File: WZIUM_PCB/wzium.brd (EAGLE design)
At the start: 100 x 100 mm, 9 parts, among them J1 RASPBERRYPI-40-PIN-GPIO_PTH

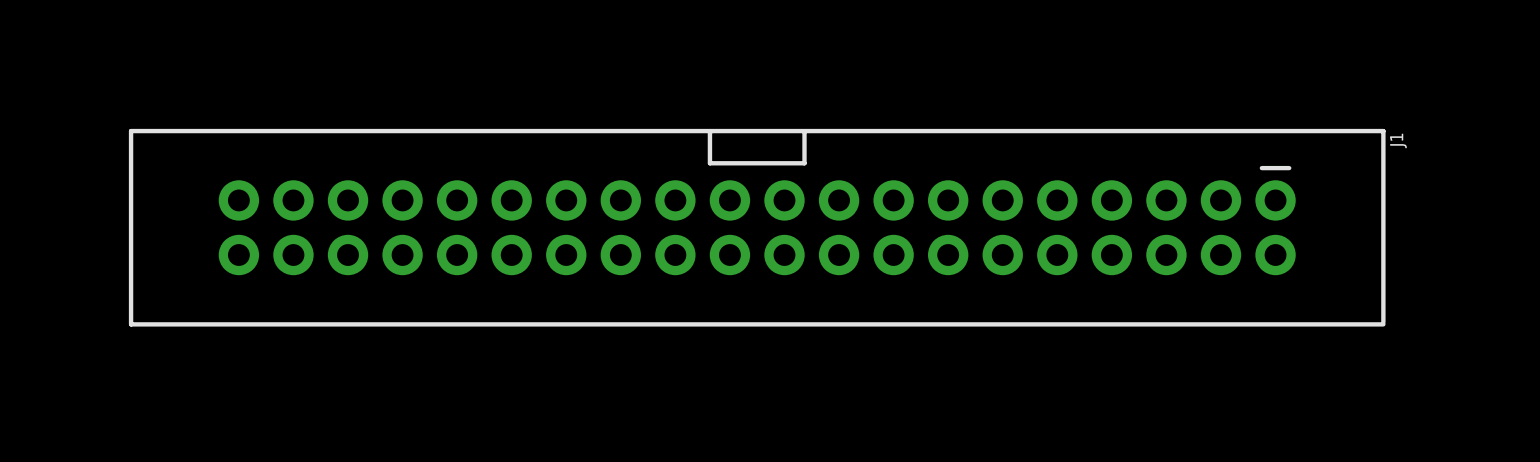
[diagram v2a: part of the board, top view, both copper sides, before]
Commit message: [FIX][ADD][PCB] Naprawiłem kolejnośc pinów od RPi na PCB | dodałem obrys RPi,
piny od RPi na 100% będą właśnie w tej konfiguracji. Obrazek na płytce póki co może być mylący, bo gniazdo FC 40p powinno mieć "ząbek" po drugiej stronie, ale postaram się to naprawić później. Dodałem też obrys RPi, dla łatwiejszego wyobrażania sobie jak to będzie wyglądało.
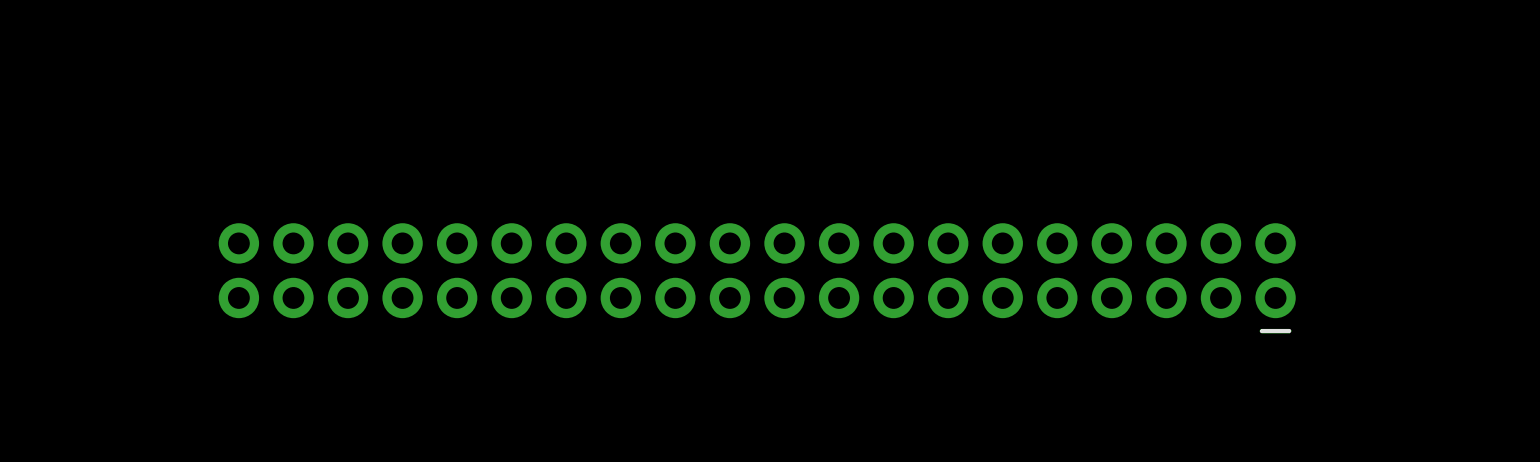
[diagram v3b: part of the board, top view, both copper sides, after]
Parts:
- moved J1 2.00 mm to (44.0, 41.0), flipped to the bottom, turned to 90 degrees
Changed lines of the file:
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@@
 <dimension x1="14.675" y1="77.375" x2="14.725" y2="28.375" x3="-2" y3="52.875" textsize="1.016" layer="1" dtype="vertical" width="0.05"/>
 <dimension x1="14.8" y1="75.775" x2="14.7" y2="29.975" x3="2" y3="52.875" textsize="1.016" layer="1" dtype="vertical" width="0.05"/>
+<wire x1="-8.825" y1="24.875" x2="-8.825" y2="80.875" width="0.1" layer="49"/>
+<wire x1="-8.825" y1="80.875" x2="76.175" y2="80.875" width="0.1" layer="49"/>
+<wire x1="76.175" y1="80.875" x2="76.175" y2="24.875" width="0.1" layer="49"/>
+<wire x1="76.175" y1="24.875" x2="-8.825" y2="24.875" width="0.1" layer="49"/>
 </plain>
 <attributes>
@@
 </autorouter>
 <elements>
-<element name="J1" library="SparkFun-Connectors" library_urn="urn:adsk.eagle:library:513" package="2X20_SHROUDED" package3d_urn="urn:adsk.eagle:package:38279/1" value="RASPBERRYPI-40-PIN-GPIO_PTH" x="44" y="43" smashed="yes" rot="R270">
-<attribute name="NAME" x="73.464" y="47.445" size="0.6096" layer="25" font="vector" ratio="20" rot="R270"/>
-<attribute name="PROD_ID" value="CONN-12263" x="44" y="43" size="1.778" layer="27" rot="R270" display="off"/>
-<attribute name="SF_ID" value="PRT-13054" x="44" y="43" size="1.778" layer="27" rot="R270" display="off"/>
-<attribute name="VALUE" x="13.901" y="47.318" size="0.6096" layer="27" font="vector" ratio="20" rot="R270"/>
+<element name="J1" library="SparkFun-Connectors" library_urn="urn:adsk.eagle:library:513" package="2X20_SHROUDED" package3d_urn="urn:adsk.eagle:package:38279/1" value="RASPBERRYPI-40-PIN-GPIO_PTH" x="44" y="41" smashed="yes" rot="MR90">
+<attribute name="NAME" x="73.464" y="36.555" size="0.6096" layer="26" font="vector" ratio="20" rot="MR90"/>
+<attribute name="PROD_ID" value="CONN-12263" x="44" y="41" size="1.778" layer="28" rot="MR90" display="off"/>
+<attribute name="SF_ID" value="PRT-13054" x="44" y="41" size="1.778" layer="28" rot="MR90" display="off"/>
+<attribute name="VALUE" x="13.901" y="36.682" size="0.6096" layer="28" font="vector" ratio="20" rot="MR90"/>
 </element>
 <element name="X1" library="con-yamaichi" library_urn="urn:adsk.eagle:library:202" package="USB-A003" package3d_urn="urn:adsk.eagle:package:11805/1" value="" x="59" y="101" smashed="yes" rot="R180">
@@
 <contactref element="J1" pad="1"/>
 <contactref element="J1" pad="17"/>
-<wire x1="47.81" y1="44.27" x2="68.13" y2="44.27" width="0" layer="19" extent="1-1"/>
+<wire x1="47.81" y1="39.73" x2="68.13" y2="39.73" width="0" layer="19" extent="1-1"/>
 </signal>
 <signal name="GND">
@@
 <contactref element="X1" pad="1"/>
 <wire x1="44.05" y1="81" x2="62.5" y2="87" width="0" layer="19" extent="1-1"/>
-<wire x1="37.65" y1="44.27" x2="44.05" y2="81" width="0" layer="19" extent="1-1"/>
-<wire x1="32.57" y1="41.73" x2="37.65" y2="44.27" width="0" layer="19" extent="1-1"/>
-<wire x1="27.49" y1="41.73" x2="32.57" y2="41.73" width="0" layer="19" extent="1-1"/>
-<wire x1="45.27" y1="41.73" x2="37.65" y2="44.27" width="0" layer="19" extent="1-1"/>
-<wire x1="52.89" y1="41.73" x2="45.27" y2="41.73" width="0" layer="19" extent="1-1"/>
-<wire x1="57.97" y1="44.27" x2="52.89" y2="41.73" width="0" layer="19" extent="1-1"/>
-<wire x1="63.05" y1="41.73" x2="57.97" y2="44.27" width="0" layer="19" extent="1-1"/>
-<wire x1="19.87" y1="44.27" x2="27.49" y2="41.73" width="0" layer="19" extent="1-1"/>
-<wire x1="95.97" y1="23" x2="63.05" y2="41.73" width="0" layer="19" extent="1-1"/>
+<wire x1="45.27" y1="42.27" x2="44.05" y2="81" width="0" layer="19" extent="1-1"/>
+<wire x1="52.89" y1="42.27" x2="45.27" y2="42.27" width="0" layer="19" extent="1-1"/>
+<wire x1="57.97" y1="39.73" x2="52.89" y2="42.27" width="0" layer="19" extent="1-1"/>
+<wire x1="63.05" y1="42.27" x2="57.97" y2="39.73" width="0" layer="19" extent="1-1"/>
+<wire x1="37.65" y1="39.73" x2="45.27" y2="42.27" width="0" layer="19" extent="1-1"/>
+<wire x1="32.57" y1="42.27" x2="37.65" y2="39.73" width="0" layer="19" extent="1-1"/>
+<wire x1="27.49" y1="42.27" x2="32.57" y2="42.27" width="0" layer="19" extent="1-1"/>
+<wire x1="19.87" y1="39.73" x2="27.49" y2="42.27" width="0" layer="19" extent="1-1"/>
+<wire x1="95.97" y1="23" x2="63.05" y2="42.27" width="0" layer="19" extent="1-1"/>
 </signal>
 <signal name="5V">
@@
 <contactref element="J1" pad="2"/>
 <contactref element="F2" pad="1"/>
-<wire x1="65.59" y1="41.73" x2="22.7478" y2="91" width="0" layer="19" extent="1-1"/>
-<wire x1="68.13" y1="41.73" x2="65.59" y2="41.73" width="0" layer="19" extent="1-1"/>
+<wire x1="65.59" y1="42.27" x2="68.13" y2="42.27" width="0" layer="19" extent="1-1"/>
+<wire x1="22.7478" y1="91" x2="65.59" y2="42.27" width="0" layer="19" extent="1-1"/>
 </signal>
 <signal name="VIN">

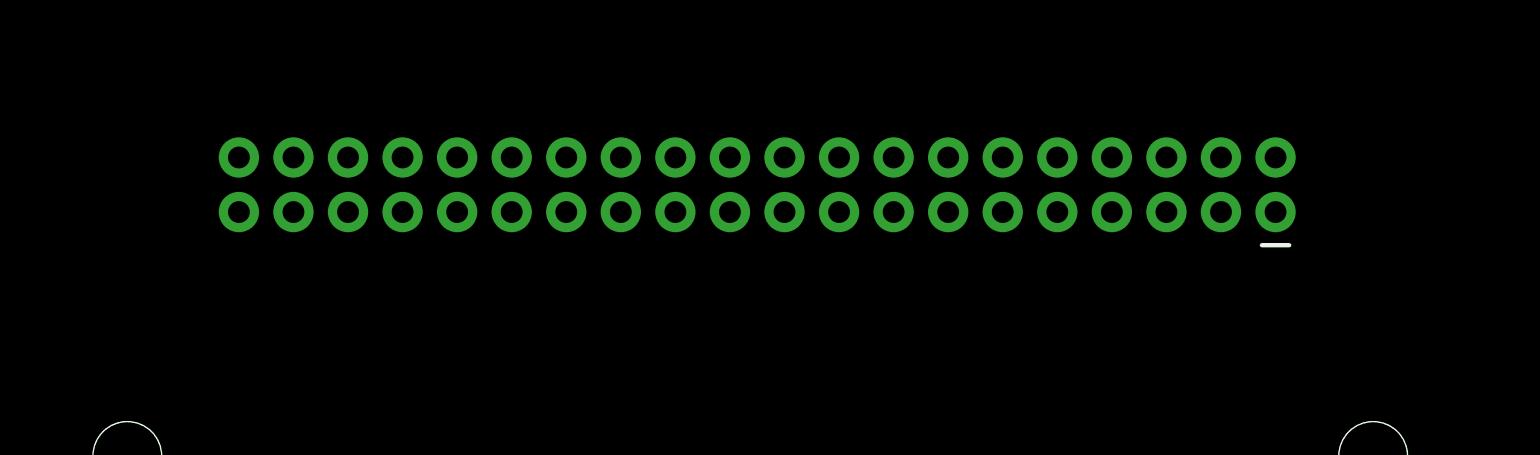
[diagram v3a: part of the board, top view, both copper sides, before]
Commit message: [FIX][PCB] Poprawiłem obrys gniazda FC 40p
Potwierdzam też kolejność pinów w tym gnieździe, zgadza się i jest ok
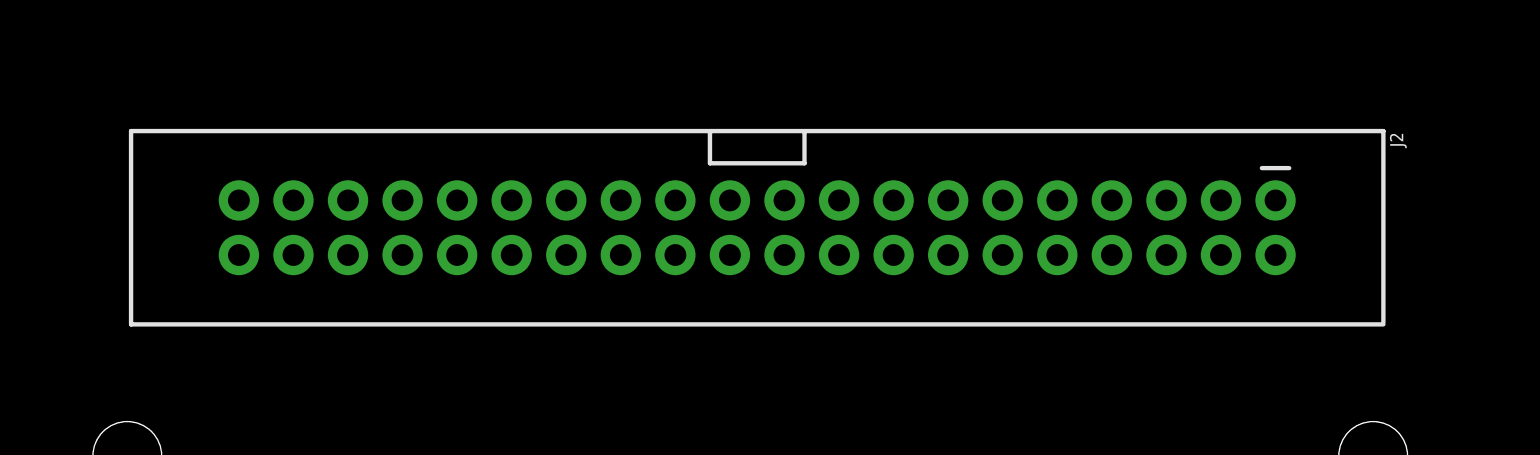
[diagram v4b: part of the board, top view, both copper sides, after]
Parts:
- removed J1: RASPBERRYPI-40-PIN-GPIO_PTH, SparkFun-Connectors:2X20_SHROUDED
- added J2: RASPBERRYPI-40-PIN-GPIO_PTH_MIRROR, _Raspberry_Pi:2X20_SHROUDED
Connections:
- net 3.3V: now also J2.18, J2.2; no longer J1.1, J1.17
- net 5V: now also J2.1, J2.3; no longer J1.2, J1.4
- net GND: now also J2.10, J2.13, J2.19, J2.26, J2.29, J2.33, J2.40, J2.5; no longer J1.14, J1.20, J1.25, J1.30, J1.34, J1.39, J1.6, J1.9
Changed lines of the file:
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@@
 </autorouter>
 <elements>
-<element name="J1" library="SparkFun-Connectors" library_urn="urn:adsk.eagle:library:513" package="2X20_SHROUDED" package3d_urn="urn:adsk.eagle:package:38279/1" value="RASPBERRYPI-40-PIN-GPIO_PTH" x="44" y="41" smashed="yes" rot="MR90">
-<attribute name="NAME" x="73.464" y="36.555" size="0.6096" layer="26" font="vector" ratio="20" rot="MR90"/>
-<attribute name="PROD_ID" value="CONN-12263" x="44" y="41" size="1.778" layer="28" rot="MR90" display="off"/>
-<attribute name="SF_ID" value="PRT-13054" x="44" y="41" size="1.778" layer="28" rot="MR90" display="off"/>
-<attribute name="VALUE" x="13.901" y="36.682" size="0.6096" layer="28" font="vector" ratio="20" rot="MR90"/>
-</element>
 <element name="X1" library="con-yamaichi" library_urn="urn:adsk.eagle:library:202" package="USB-A003" package3d_urn="urn:adsk.eagle:package:11805/1" value="" x="59" y="101" smashed="yes" rot="R180">
 <attribute name="MF" value="" x="59" y="101" size="1.778" layer="27" rot="R180" display="off"/>
@@
 <element name="U$4" library="_MOUNTING_HOLES" package="M3-HOLE" value="" x="72.675" y="77.375" smashed="yes"/>
 <element name="U$3" library="_MOUNTING_HOLES" package="M3-HOLE" value="" x="14.675" y="77.375" smashed="yes"/>
+<element name="J2" library="_Raspberry_Pi" package="2X20_SHROUDED" value="RASPBERRYPI-40-PIN-GPIO_PTH_MIRROR" x="44" y="39" smashed="yes" rot="R270">
+<attribute name="NAME" x="73.464" y="43.445" size="0.6096" layer="25" font="vector" ratio="20" rot="R270"/>
+<attribute name="PROD_ID" value="CONN-12263" x="44" y="39" size="1.778" layer="27" rot="R270" display="off"/>
+<attribute name="SF_ID" value="PRT-13054" x="44" y="39" size="1.778" layer="27" rot="R270" display="off"/>
+<attribute name="VALUE" x="13.901" y="43.318" size="0.6096" layer="27" font="vector" ratio="20" rot="R270"/>
+</element>
 </elements>
 <signals>
 <signal name="3.3V">
-<contactref element="J1" pad="1"/>
-<contactref element="J1" pad="17"/>
-<wire x1="47.81" y1="39.73" x2="68.13" y2="39.73" width="0" layer="19" extent="1-1"/>
+<contactref element="J2" pad="2"/>
+<contactref element="J2" pad="18"/>
+<wire x1="47.81" y1="37.73" x2="68.13" y2="37.73" width="0" layer="19" extent="1-1"/>
 </signal>
 <signal name="GND">
-<contactref element="J1" pad="9"/>
-<contactref element="J1" pad="25"/>
-<contactref element="J1" pad="20"/>
-<contactref element="J1" pad="14"/>
-<contactref element="J1" pad="6"/>
-<contactref element="J1" pad="30"/>
-<contactref element="J1" pad="34"/>
-<contactref element="J1" pad="39"/>
 <contactref element="U$9" pad="1"/>
 <contactref element="BATTERY" pad="1"/>
 <contactref element="X1" pad="1"/>
+<contactref element="J2" pad="10"/>
+<contactref element="J2" pad="26"/>
+<contactref element="J2" pad="19"/>
+<contactref element="J2" pad="13"/>
+<contactref element="J2" pad="5"/>
+<contactref element="J2" pad="29"/>
+<contactref element="J2" pad="33"/>
+<contactref element="J2" pad="40"/>
 <wire x1="44.05" y1="81" x2="62.5" y2="87" width="0" layer="19" extent="1-1"/>
-<wire x1="45.27" y1="42.27" x2="44.05" y2="81" width="0" layer="19" extent="1-1"/>
-<wire x1="52.89" y1="42.27" x2="45.27" y2="42.27" width="0" layer="19" extent="1-1"/>
-<wire x1="57.97" y1="39.73" x2="52.89" y2="42.27" width="0" layer="19" extent="1-1"/>
-<wire x1="63.05" y1="42.27" x2="57.97" y2="39.73" width="0" layer="19" extent="1-1"/>
-<wire x1="37.65" y1="39.73" x2="45.27" y2="42.27" width="0" layer="19" extent="1-1"/>
-<wire x1="32.57" y1="42.27" x2="37.65" y2="39.73" width="0" layer="19" extent="1-1"/>
-<wire x1="27.49" y1="42.27" x2="32.57" y2="42.27" width="0" layer="19" extent="1-1"/>
-<wire x1="19.87" y1="39.73" x2="27.49" y2="42.27" width="0" layer="19" extent="1-1"/>
-<wire x1="95.97" y1="23" x2="63.05" y2="42.27" width="0" layer="19" extent="1-1"/>
+<wire x1="63.05" y1="40.27" x2="44.05" y2="81" width="0" layer="19" extent="1-1"/>
+<wire x1="57.97" y1="37.73" x2="63.05" y2="40.27" width="0" layer="19" extent="1-1"/>
+<wire x1="52.89" y1="40.27" x2="57.97" y2="37.73" width="0" layer="19" extent="1-1"/>
+<wire x1="45.27" y1="40.27" x2="52.89" y2="40.27" width="0" layer="19" extent="1-1"/>
+<wire x1="37.65" y1="37.73" x2="45.27" y2="40.27" width="0" layer="19" extent="1-1"/>
+<wire x1="32.57" y1="40.27" x2="37.65" y2="37.73" width="0" layer="19" extent="1-1"/>
+<wire x1="27.49" y1="40.27" x2="32.57" y2="40.27" width="0" layer="19" extent="1-1"/>
+<wire x1="19.87" y1="37.73" x2="27.49" y2="40.27" width="0" layer="19" extent="1-1"/>
+<wire x1="95.97" y1="23" x2="62.5" y2="87" width="0" layer="19" extent="1-1"/>
 </signal>
 <signal name="5V">
-<contactref element="J1" pad="4"/>
-<contactref element="J1" pad="2"/>
 <contactref element="F2" pad="1"/>
-<wire x1="65.59" y1="42.27" x2="68.13" y2="42.27" width="0" layer="19" extent="1-1"/>
-<wire x1="22.7478" y1="91" x2="65.59" y2="42.27" width="0" layer="19" extent="1-1"/>
+<contactref element="J2" pad="3"/>
+<contactref element="J2" pad="1"/>
+<wire x1="68.13" y1="40.27" x2="22.7478" y2="91" width="0" layer="19" extent="1-1"/>
+<wire x1="65.59" y1="40.27" x2="68.13" y2="40.27" width="0" layer="19" extent="1-1"/>
 </signal>
 <signal name="VIN">

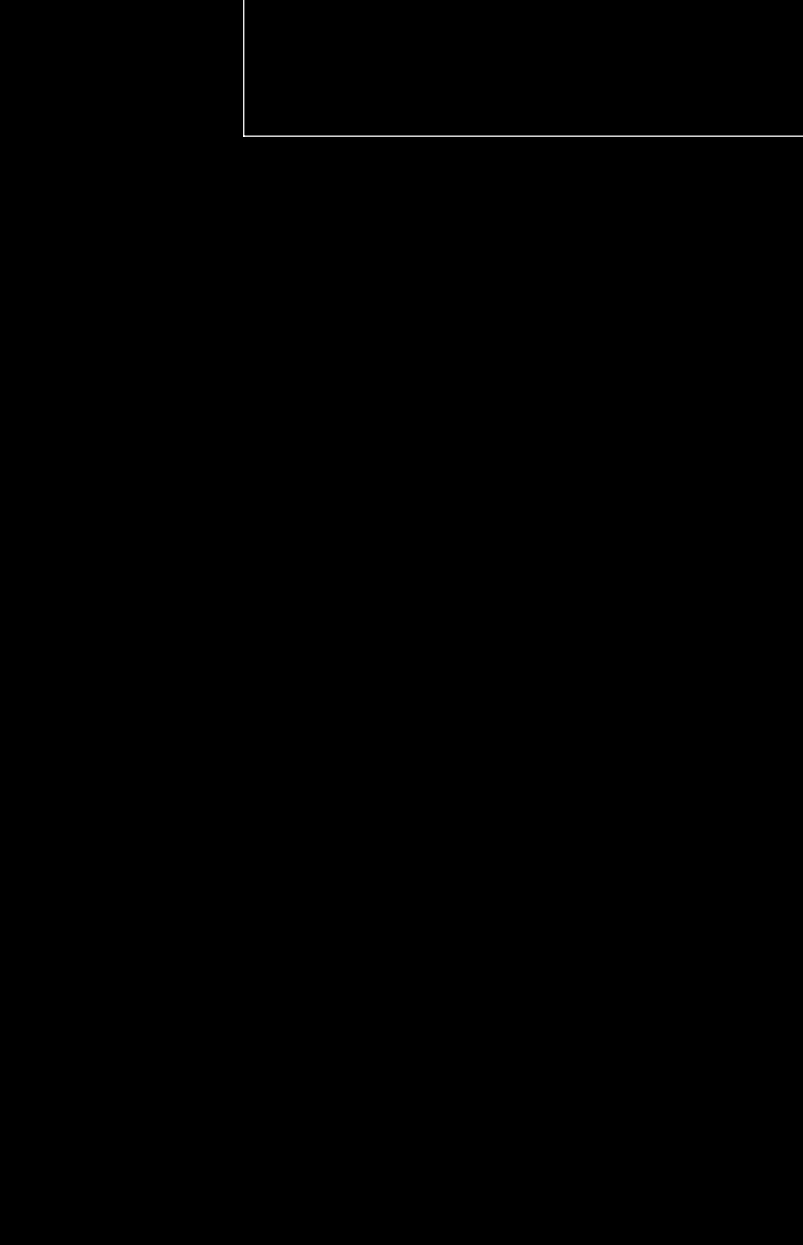
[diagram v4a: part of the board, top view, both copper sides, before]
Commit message: dodanie sekcji sterowania silnikiem i AVR, dodanie .gitignore
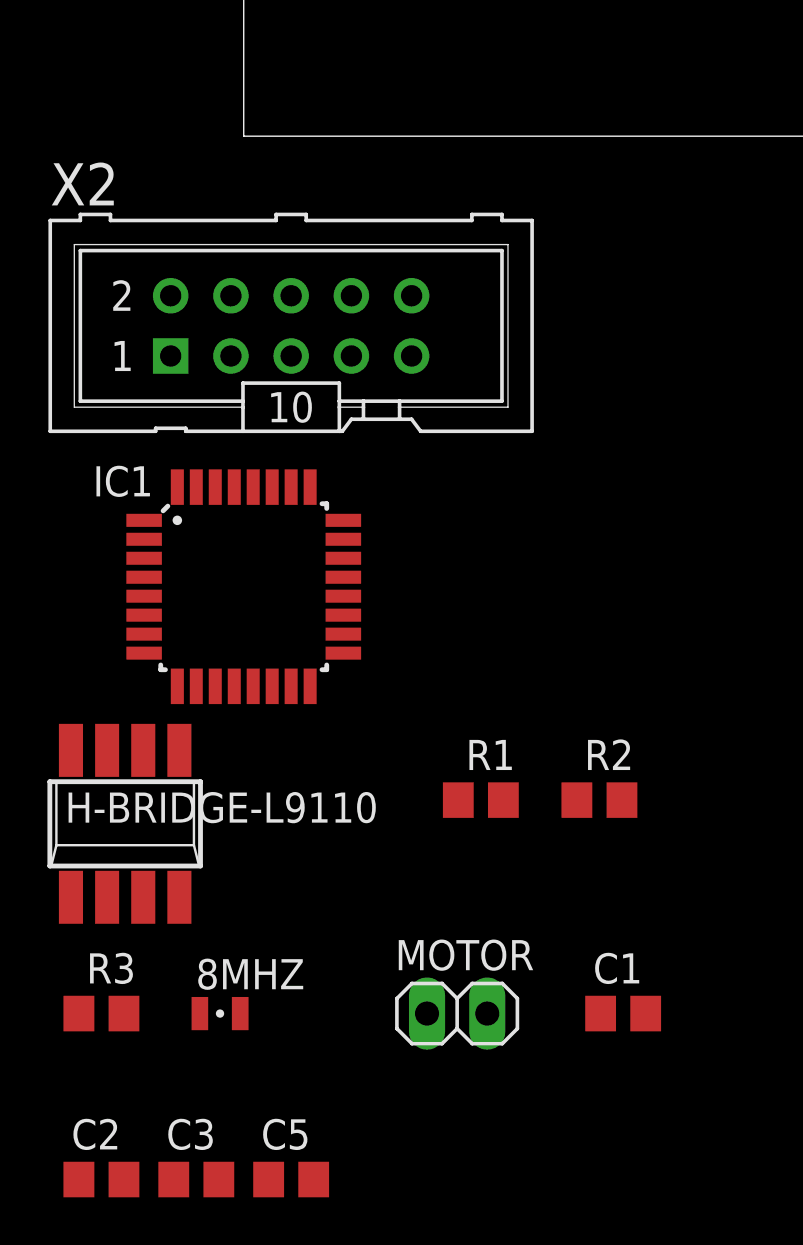
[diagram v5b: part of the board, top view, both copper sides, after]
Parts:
- added 8MHZ: FC-12M, crystal:FC-12M
- added C1, C2, C3, C5: (no value), rcl:C0805
- added H-BRIDGE-L9110: (no value), zetex:SM8
- added IC1: ATMEGA328PB-AU, atmel:QFP32_7X7_0.80
- added MOTOR: (no value), DC_LOAD_AU:1X02
- added R1, R2, R3: 10k, rcl:R0805
- added X2: (no value), atmel:IDC-10V
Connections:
- new net 7.2V: H-BRIDGE-L9110.2, H-BRIDGE-L9110.3
- new net CLK: IC1.17, X2.7
- new net IN_BACKWARD: IC1.10, R2.1
- new net IN_FORWARD: IC1.9, R1.2
- new net MISO: IC1.16, X2.9
- new net MOSI: IC1.15, X2.1
- new net N$3: H-BRIDGE-L9110.7, R2.2
- new net N$5: H-BRIDGE-L9110.6, R1.1
- new net N$7: 8MHZ.1, C3.1, IC1.7
- new net N$8: 8MHZ.2, C2.1, IC1.8
- new net OUT1: C1.2, H-BRIDGE-L9110.1, MOTOR.1
- new net OUT2: C1.1, H-BRIDGE-L9110.4, MOTOR.2
- new net RESET: IC1.29, R3.2, X2.5
- new net VCC: C5.1, IC1.18, IC1.4, R3.1, X2.2
- net GND: now also C2.2, C3.2, C5.2, H-BRIDGE-L9110.5, H-BRIDGE-L9110.8, IC1.21, IC1.5, X2.10, X2.4, X2.6, X2.8
